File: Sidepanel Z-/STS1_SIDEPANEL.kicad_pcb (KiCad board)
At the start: 4 copper layers, 82.8 x 100 mm, 32 parts, among them IC1 TMP112AQDRLRQ1, J1 Conn_01x18, J3 Conn_01x12, U1 GUVA-C32SM, U11 INA180A4

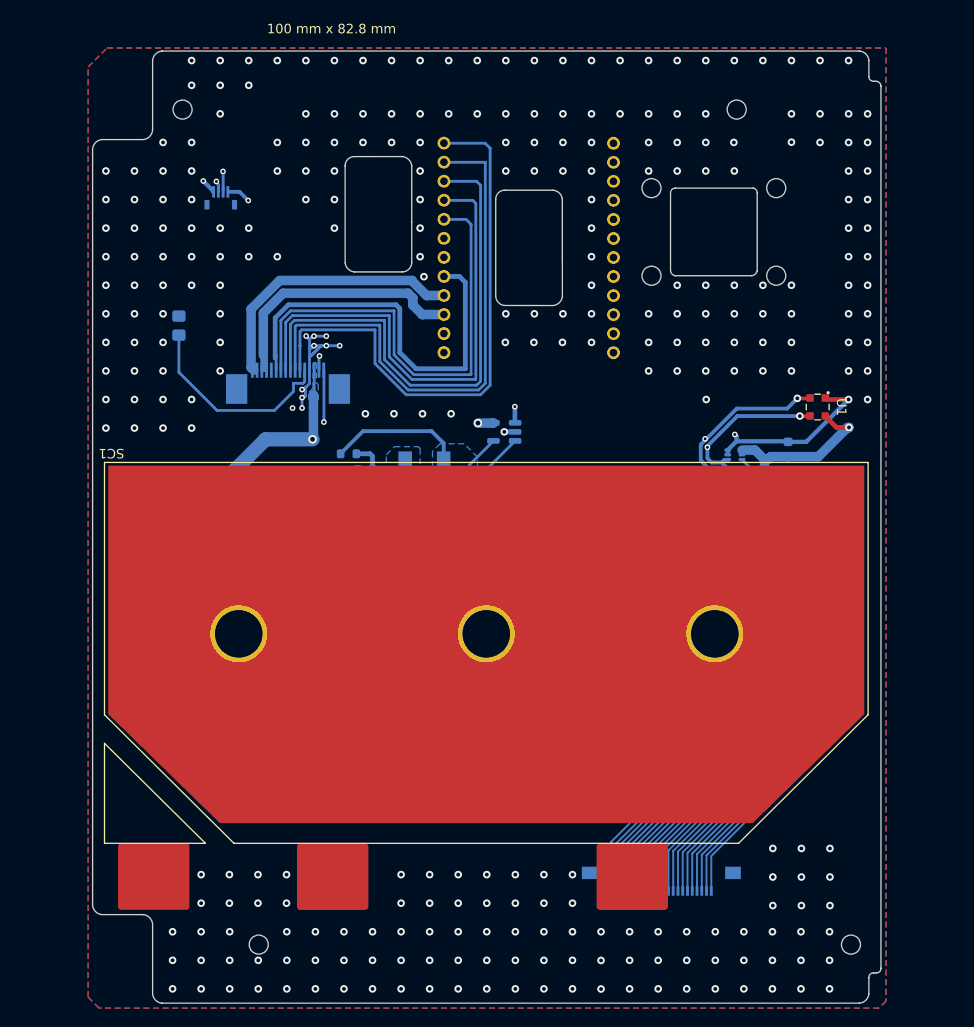
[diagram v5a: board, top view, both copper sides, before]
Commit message: moved the connectors, changed the footprint of the input and output capacitors and splitted the input capacitor in two
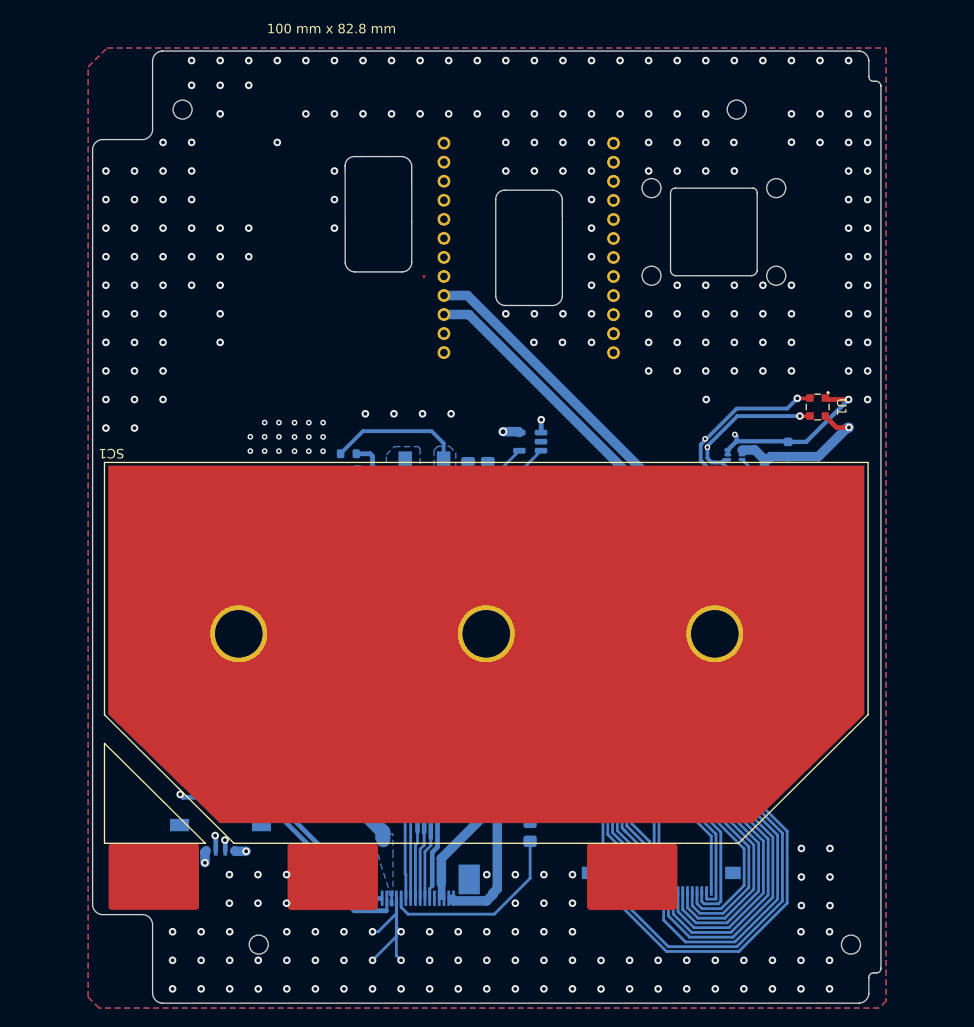
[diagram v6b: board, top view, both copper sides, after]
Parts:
- C11, C61: value 10u -> 22u; footprint Capacitor_SMD:C_0603_1608Metric -> Capacitor_SMD:C_0805_2012Metric
- C41: value 4u7 -> 22u; footprint Capacitor_SMD:C_0603_1608Metric -> Capacitor_SMD:C_0805_2012Metric
- R11: footprint Resistor_SMD:R_0603_1608Metric -> Resistor_SMD:R_0805_2012Metric
- R51: value 0R01 -> 220m; footprint Resistor_SMD:R_0603_1608Metric -> Resistor_SMD:R_0805_2012Metric
- UV1: footprint STS_connector:5014610491 -> STS_connector:200528-0040
- moved UV1 68.3 mm to (97.0, 123.5), turned to 0 degrees
- moved TH1 64.7 mm to (129.6, 121.5)
- moved J1 53.3 mm to (117.8, 126.5), turned to 0 degrees
- moved C61 18.2 mm to (125.1, 83.6), turned to 90 degrees
- moved C11 6.32 mm to (123.0, 83.6), turned to 90 degrees
- moved R11 4.11 mm to (127.8, 86.3)
- moved U11 2.91 mm to (129.6, 80.5)
- moved R71 1.59 mm to (105.3, 89.5)
- moved R61 1.53 mm to (103.7, 89.5)
- moved C31 1.17 mm to (106.9, 89.4), turned to -90 degrees
- moved D21 0.47 mm to (113.3, 93.6)
- moved R51 0.22 mm to (110.8, 91.2)
- moved C41 0.18 mm to (114.9, 91.3)
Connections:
- C61 pad 1: /MPPT1 -> /SolarMPPT/CUR1_OUT
- edu_con1 pad 1: Net-(cam1-Pad1) -> Net-(cam1-Pad22)
- edu_con1 pad 10: Net-(cam1-Pad10) -> Net-(cam1-Pad13)
- edu_con1 pad 11: Net-(cam1-Pad11) -> Net-(cam1-Pad12)
- edu_con1 pad 12: Net-(cam1-Pad12) -> Net-(cam1-Pad11)
- edu_con1 pad 13: Net-(cam1-Pad13) -> Net-(cam1-Pad10)
- edu_con1 pad 14: Net-(cam1-Pad14) -> Net-(cam1-Pad9)
- edu_con1 pad 15: Net-(cam1-Pad15) -> Net-(cam1-Pad8)
- edu_con1 pad 16: Net-(cam1-Pad16) -> Net-(cam1-Pad7)
- edu_con1 pad 17: Net-(cam1-Pad17) -> Net-(cam1-Pad6)
- edu_con1 pad 18: Net-(cam1-Pad18) -> Net-(cam1-Pad5)
- edu_con1 pad 19: Net-(cam1-Pad19) -> Net-(cam1-Pad4)
- edu_con1 pad 2: Net-(cam1-Pad2) -> Net-(cam1-Pad21)
- edu_con1 pad 20: Net-(cam1-Pad20) -> Net-(cam1-Pad3)
- edu_con1 pad 21: Net-(cam1-Pad21) -> Net-(cam1-Pad2)
- edu_con1 pad 22: Net-(cam1-Pad22) -> Net-(cam1-Pad1)
- edu_con1 pad 3: Net-(cam1-Pad3) -> Net-(cam1-Pad20)
- edu_con1 pad 4: Net-(cam1-Pad4) -> Net-(cam1-Pad19)
- edu_con1 pad 5: Net-(cam1-Pad5) -> Net-(cam1-Pad18)
- edu_con1 pad 6: Net-(cam1-Pad6) -> Net-(cam1-Pad17)
- edu_con1 pad 7: Net-(cam1-Pad7) -> Net-(cam1-Pad16)
- edu_con1 pad 8: Net-(cam1-Pad8) -> Net-(cam1-Pad15)
- edu_con1 pad 9: Net-(cam1-Pad9) -> Net-(cam1-Pad14)
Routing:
- net /SC1_I+: track 25.9 -> 105.2 mm
- net /COBC_NOT_RST: track 55.0 -> 125.6 mm, vias 0 -> 1
- net /UART_TX: track 57.5 -> 126.3 mm, vias 0 -> 1
- net /UART_RX: track 59.4 -> 127.2 mm, vias 0 -> 1
- net /COBC_SWDCLK: track 49.9 -> 115.3 mm, vias 0 -> 1
- net /COBC_SWDIO: track 52.6 -> 117.7 mm, vias 0 -> 1
- net +5V: track 43.4 -> 108.1 mm, vias 0 -> 1
- net /Bat+: track 28.7 -> 90.2 mm, vias 0 -> 2
- net /Bat-: track 31.1 -> 88.5 mm, vias 0 -> 2
- net /SC1_V+: track 78.4 -> 42.7 mm
- net Net-(cam1-Pad21): track 17.0 -> 40.5 mm
- net Net-(cam1-Pad22): track 17.0 -> 40.2 mm
- net Net-(cam1-Pad20): track 17.0 -> 38.8 mm
- net Net-(cam1-Pad19): track 17.0 -> 38.5 mm
- net Net-(cam1-Pad18): track 17.0 -> 36.9 mm
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
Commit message: Z- Cam Connerctor Rerout, add vias & 90deg trace removal
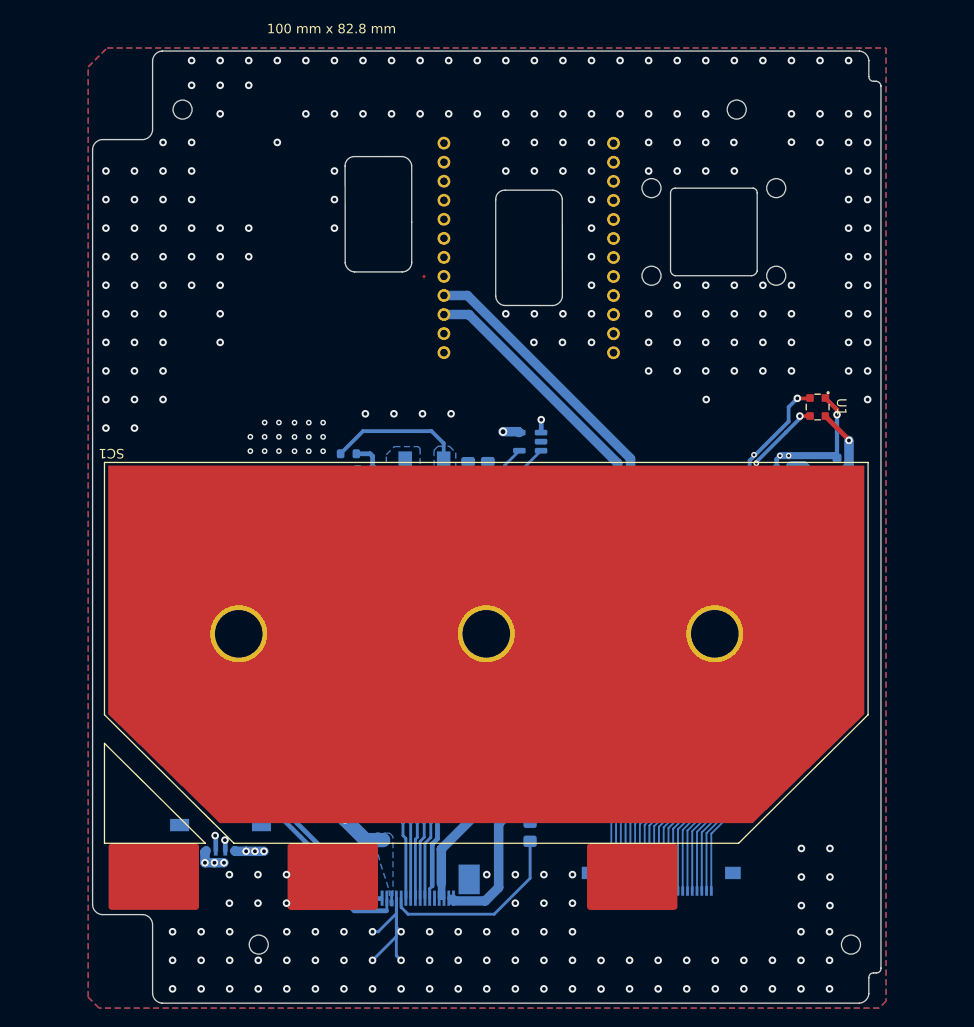
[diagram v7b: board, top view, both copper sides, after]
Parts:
- moved IC1 5.40 mm to (156.2, 83.6)
- moved C1 5.40 mm to (161.8, 83.0)
- moved RU1 5.40 mm to (157.6, 88.0)
- moved RU2 5.40 mm to (155.6, 88.0)
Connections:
- edu_con1 pad 1: Net-(cam1-Pad22) -> Net-(cam1-Pad1)
- edu_con1 pad 10: Net-(cam1-Pad13) -> Net-(cam1-Pad10)
- edu_con1 pad 11: Net-(cam1-Pad12) -> Net-(cam1-Pad11)
- edu_con1 pad 12: Net-(cam1-Pad11) -> Net-(cam1-Pad12)
- edu_con1 pad 13: Net-(cam1-Pad10) -> Net-(cam1-Pad13)
- edu_con1 pad 14: Net-(cam1-Pad9) -> Net-(cam1-Pad14)
- edu_con1 pad 15: Net-(cam1-Pad8) -> Net-(cam1-Pad15)
- edu_con1 pad 16: Net-(cam1-Pad7) -> Net-(cam1-Pad16)
- edu_con1 pad 17: Net-(cam1-Pad6) -> Net-(cam1-Pad17)
- edu_con1 pad 18: Net-(cam1-Pad5) -> Net-(cam1-Pad18)
- edu_con1 pad 19: Net-(cam1-Pad4) -> Net-(cam1-Pad19)
- edu_con1 pad 2: Net-(cam1-Pad21) -> Net-(cam1-Pad2)
- edu_con1 pad 20: Net-(cam1-Pad3) -> Net-(cam1-Pad20)
- edu_con1 pad 21: Net-(cam1-Pad2) -> Net-(cam1-Pad21)
- edu_con1 pad 22: Net-(cam1-Pad1) -> Net-(cam1-Pad22)
- edu_con1 pad 3: Net-(cam1-Pad20) -> Net-(cam1-Pad3)
- edu_con1 pad 4: Net-(cam1-Pad19) -> Net-(cam1-Pad4)
- edu_con1 pad 5: Net-(cam1-Pad18) -> Net-(cam1-Pad5)
- edu_con1 pad 6: Net-(cam1-Pad17) -> Net-(cam1-Pad6)
- edu_con1 pad 7: Net-(cam1-Pad16) -> Net-(cam1-Pad7)
- edu_con1 pad 8: Net-(cam1-Pad15) -> Net-(cam1-Pad8)
- edu_con1 pad 9: Net-(cam1-Pad14) -> Net-(cam1-Pad9)
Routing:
- net Net-(cam1-Pad21): track 40.5 -> 17.0 mm
- net Net-(cam1-Pad22): track 40.2 -> 17.0 mm
- net Net-(cam1-Pad20): track 38.8 -> 17.0 mm
- net Net-(cam1-Pad19): track 38.5 -> 17.0 mm
- net Net-(cam1-Pad18): track 36.9 -> 17.0 mm
- net Net-(cam1-Pad11): track 36.2 -> 17.0 mm
- net Net-(cam1-Pad17): track 35.2 -> 17.0 mm
- net Net-(cam1-Pad10): track 34.4 -> 17.0 mm
- net Net-(cam1-Pad16): track 33.5 -> 17.0 mm
- net Net-(cam1-Pad9): track 32.8 -> 17.0 mm
- net Net-(cam1-Pad15): track 31.9 -> 17.0 mm
- net Net-(cam1-Pad8): track 31.1 -> 17.0 mm
- net Net-(cam1-Pad14): track 30.2 -> 17.0 mm
- net Net-(cam1-Pad7): track 29.5 -> 17.0 mm
- net Net-(cam1-Pad6): track 27.8 -> 17.0 mm
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
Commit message: Minor improvements. - Added some vias to current carrying traces. - Added edge outline to sidepanel z+ again. - Fixed some minor warnings.
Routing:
- net /MPPT1: track 92.3 -> 97.3 mm, vias 9 -> 11
- net /Bat-: track 91.5 -> 92.7 mm, vias 7 -> 8
- net /Bat+: track 91.8 -> 93.0 mm, vias 7 -> 8
